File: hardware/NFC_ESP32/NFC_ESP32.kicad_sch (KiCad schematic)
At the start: 62 parts, among them J1 USB_C_Receptacle_USB2.0_14P, J2 Conn_01x02, Q1 BSS138, Q2 BSS138, Q3 DMG2301L, Q5 MMBT3904, SW1 SW_SPST, U1 ESP32-WROOM-32D, U2 CH340C, U3 MCP73831-2-OT, U4 AP2112K-3.3, U5 RC522, Y1 Crystal 27.12MHz

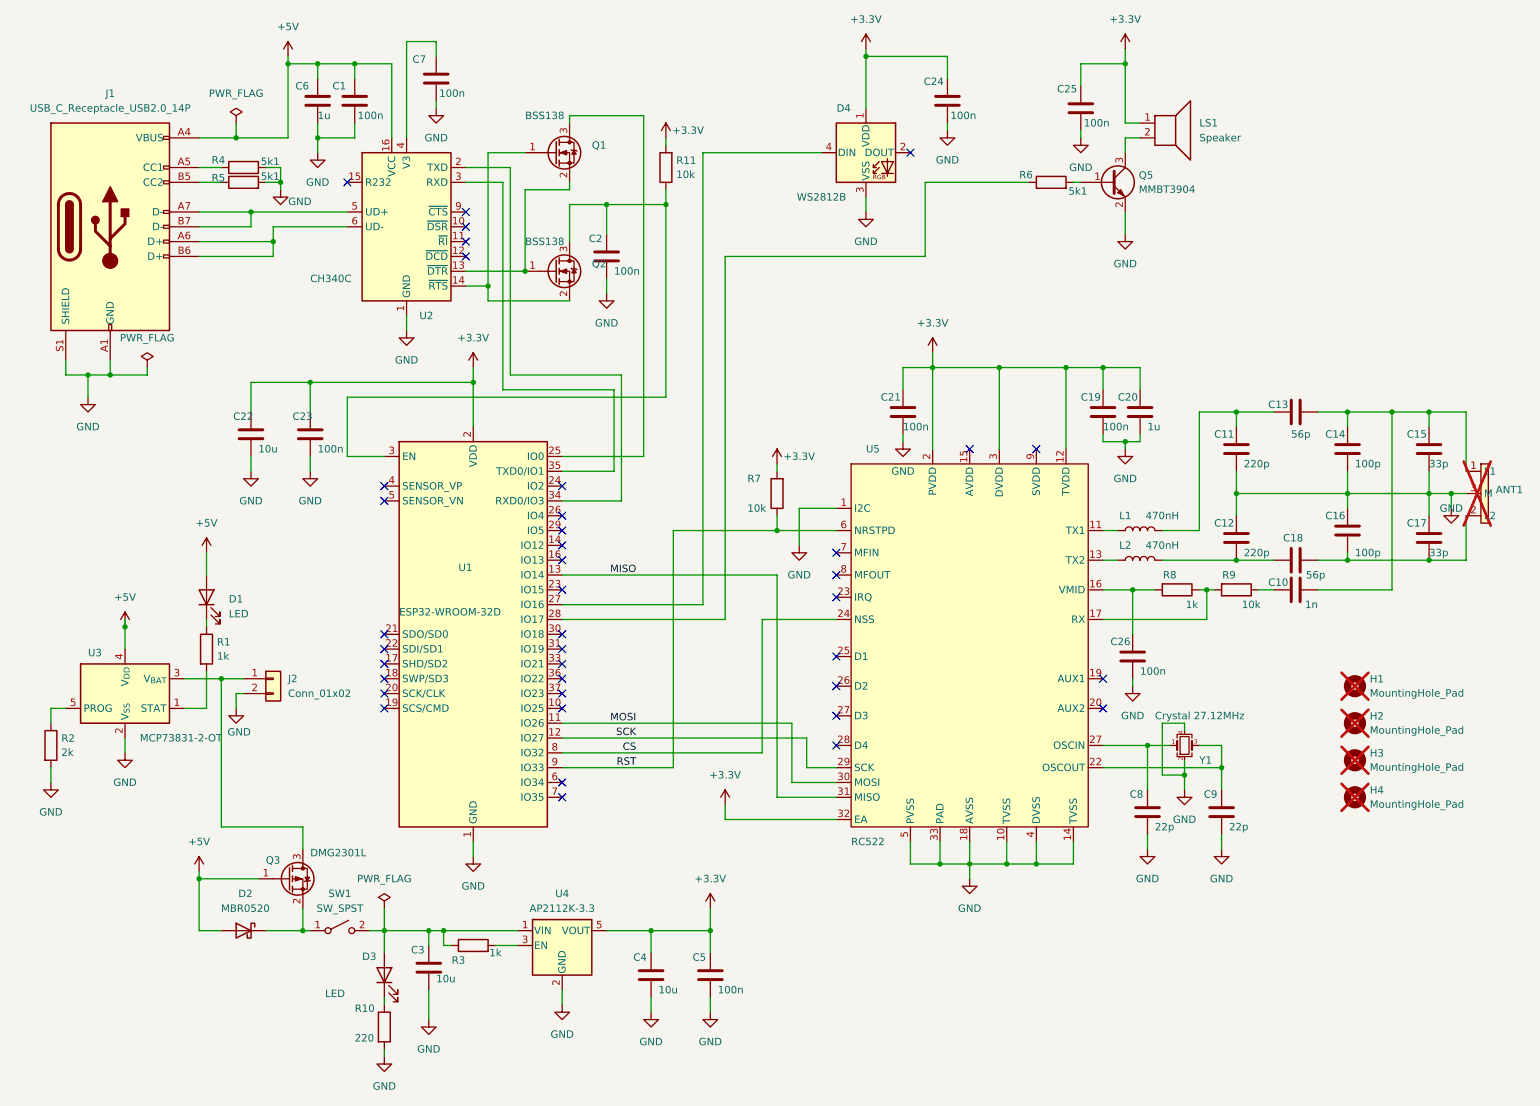
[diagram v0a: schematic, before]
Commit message: Changed to resolve issues on Version 1.0
Change RC522 symbol and fix crystal pins
Swap D- and D+
Move OLED and buzzer pins
Power AVDD on RC522
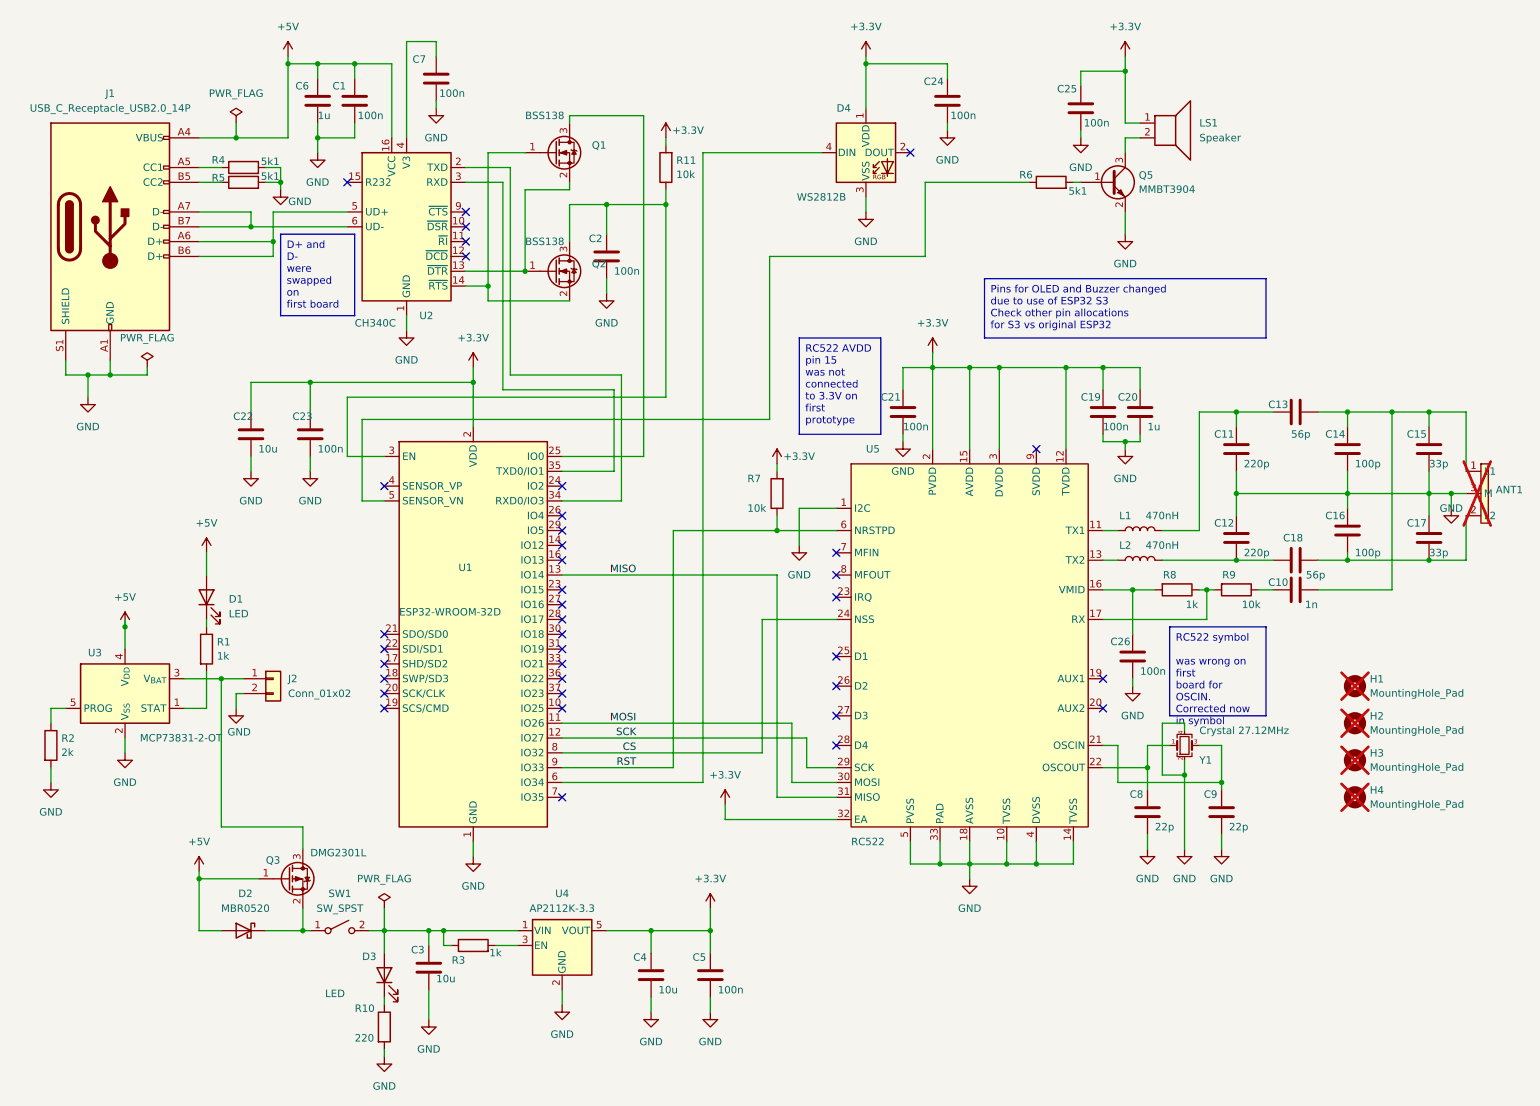
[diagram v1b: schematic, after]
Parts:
- U1: footprint RFID:ESP32-WROOM-32D -> RF_Module:ESP32-WROOM-32D
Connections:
- net +3.3V: now also U5.15 (AVDD)
- net at C8.1, Y1.1: now also U5.22 (OSCOUT); no longer U5.27 (OSCIN)
- net at C9.1, Y1.3: now also U5.21 (OSCIN); no longer U5.22 (OSCOUT)
- net at D4.4 (DIN): now also U1.6 (IO34); no longer U1.27 (IO16)
- net at R6.1: now also U1.5 (SENSOR_VN); no longer U1.28 (IO17)
- net at J1.A7 (D-), J1.B7 (D-): now also U2.6 (UD-); no longer U2.5 (UD+)
- net at J1.A6 (D+), J1.B6 (D+): now also U2.5 (UD+); no longer U2.6 (UD-)
- no-connect marks 39 -> 38
